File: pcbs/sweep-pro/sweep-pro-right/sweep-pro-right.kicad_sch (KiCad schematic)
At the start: 50 parts, among them J1 Conn_01x04_Female, J2 Conn_01x04_Female, J3 expantion1, SW1 SW_PUSH-kbd, SW10 SW_PUSH-kbd, SW11 SW_PUSH-kbd, SW12 SW_PUSH-kbd, SW13 SW_PUSH-kbd, SW14 SW_PUSH-kbd, SW15 SW_PUSH-kbd, SW16 SW_PUSH-kbd, SW17 SW_PUSH-kbd, SW2 SW_PUSH-kbd, SW3 SW_PUSH-kbd, SW4 SW_PUSH-kbd, SW5 SW_PUSH-kbd, SW6 SW_PUSH-kbd, SW7 SW_PUSH-kbd, SW8 SW_PUSH-kbd, SW9 SW_PUSH-kbd, U1 ProMicro-kbd

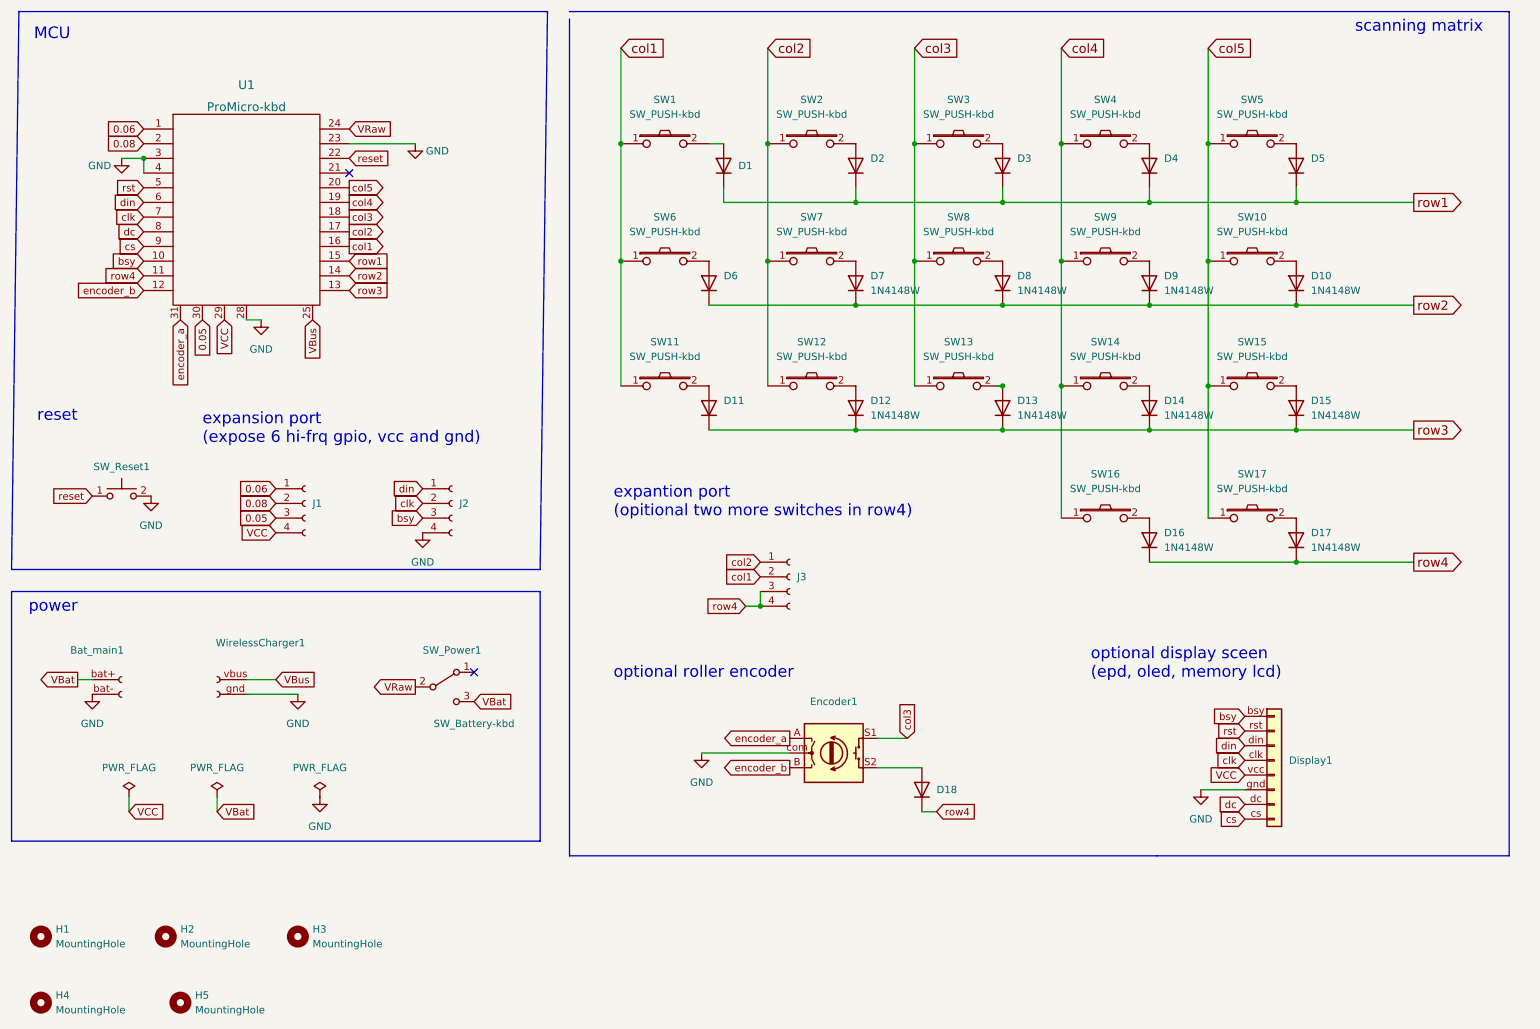
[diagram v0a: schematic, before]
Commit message: sweepro v2
1. add three expansion ports (pogopin connection)
2. remev battery extra port
3. use nrfmacro-lite partial footprint
4. new power switch
5. re-position reset button
6. seperate board for left and right split
7. more symmetric layout of the encoders
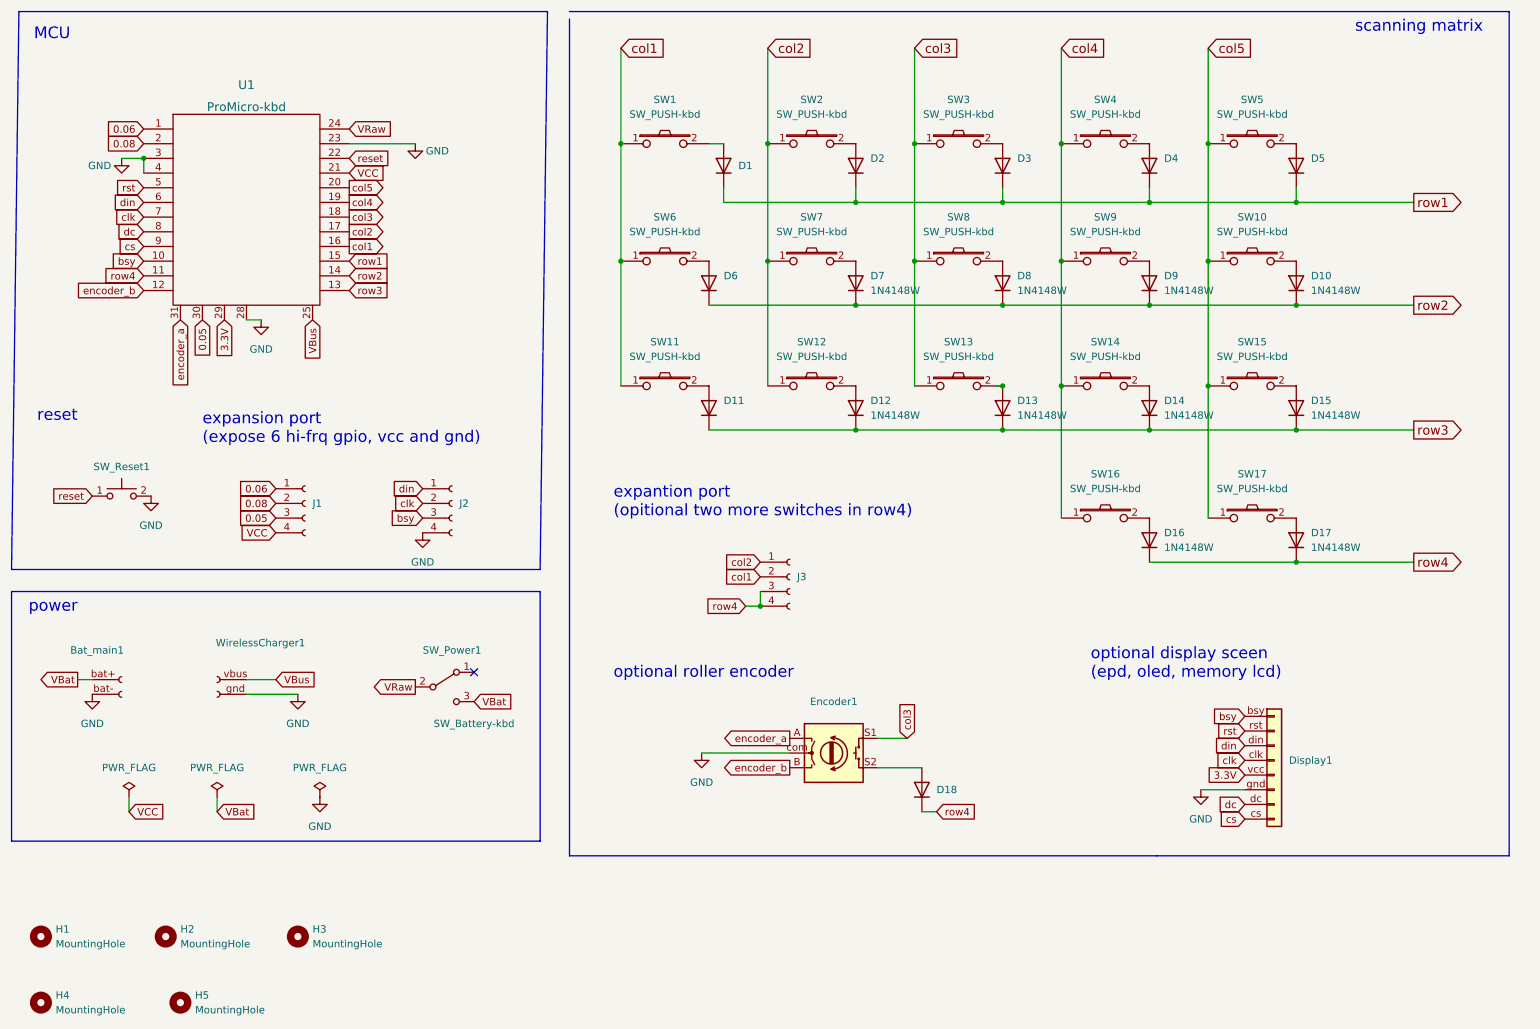
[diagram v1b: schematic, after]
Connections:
- net VCC: now also U1.21 (VCC); no longer Display1.vcc (VCC), U1.29 (3.3V)
- new net 3.3V: Display1.vcc (VCC), U1.29 (3.3V)
- no-connect marks 2 -> 1
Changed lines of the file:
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@@
   )
   (no_connect (at 100.33 130.81))
-  (no_connect (at 78.74 44.45))
   (wire (pts (xy 201.93 59.69) (xy 201.93 81.28))
     (stroke (width 0) (type default) (color 0 0 0 0))
@@
     )
   )
-  (global_label "VCC" (shape input) (at 57.15 69.85 270) (fields_autoplaced)
-    (effects (font (size 1.27 1.27)) (justify right))
-    (property "Intersheet References" "${INTERSHEET_REFS}" (id 0) (at 57.0706 75.8917 90)
+  (global_label "3.3V" (shape input) (at 57.15 69.85 270) (fields_autoplaced)
+    (effects (font (size 1.27 1.27)) (justify right))
+    (property "Intersheet References" "${INTERSHEET_REFS}" (id 0) (at 57.0706 76.3755 90)
       (effects (font (size 1.27 1.27)) (justify right) hide)
     )
@@
     )
   )
-  (global_label "VCC" (shape input) (at 233.68 148.59 180) (fields_autoplaced)
-    (effects (font (size 1.27 1.27)) (justify right))
-    (property "Intersheet References" "${INTERSHEET_REFS}" (id 0) (at 227.6383 148.5106 0)
-      (effects (font (size 1.27 1.27)) (justify right) hide)
-    )
+  (global_label "VCC" (shape input) (at 78.74 44.45 0) (fields_autoplaced)
+    (effects (font (size 1.27 1.27)) (justify left))
+    (property "Intersheet References" "${INTERSHEET_REFS}" (id 0) (at 84.7817 44.3706 0)
+      (effects (font (size 1.27 1.27)) (justify left) hide)
+    )
+  )
+  (global_label "3.3V" (shape input) (at 233.68 148.59 180) (fields_autoplaced)
+    (effects (font (size 1.27 1.27)) (justify right))
+    (property "Intersheet References" "${INTERSHEET_REFS}" (id 0) (at 227.1545 148.5106 0)
+      (effects (font (size 1.27 1.27)) (justify right) hide)
+    )
